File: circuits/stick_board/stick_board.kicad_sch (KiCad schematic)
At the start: 41 parts, among them J1 Conn_01x15_Socket, M2 Motor_DC, Q2 AO3400A, U1 GULI, U2 GULI, U5 DRV5055A1xDBZxQ1, U6 DRV5055A1xDBZxQ1

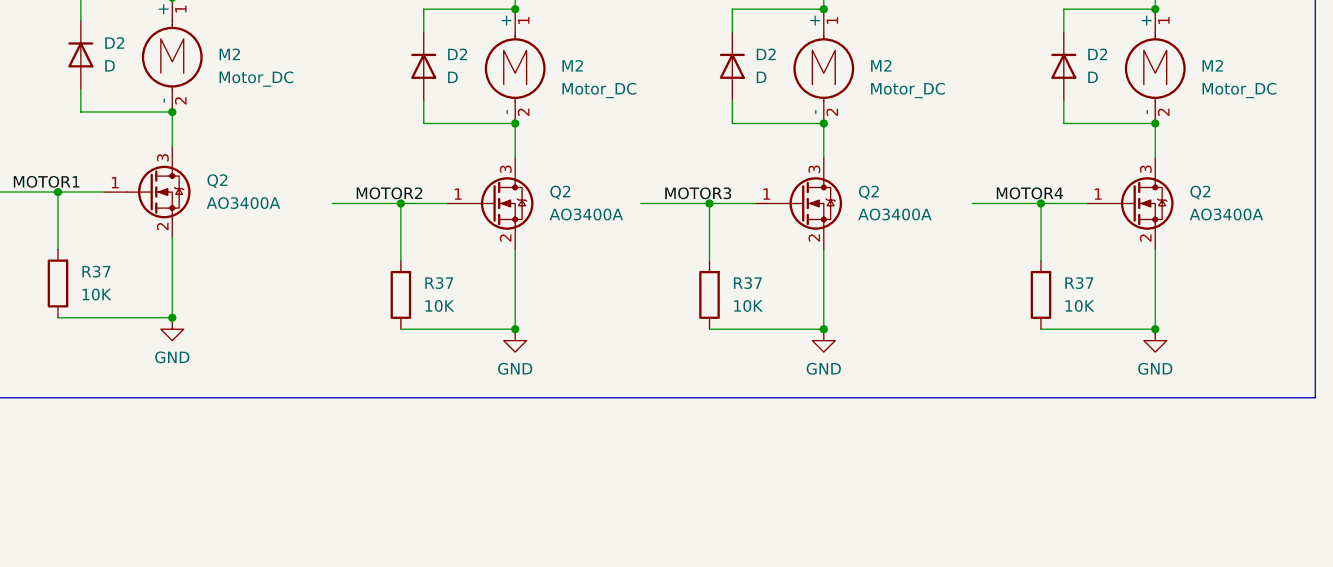
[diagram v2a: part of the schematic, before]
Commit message: 增加马达限流电阻
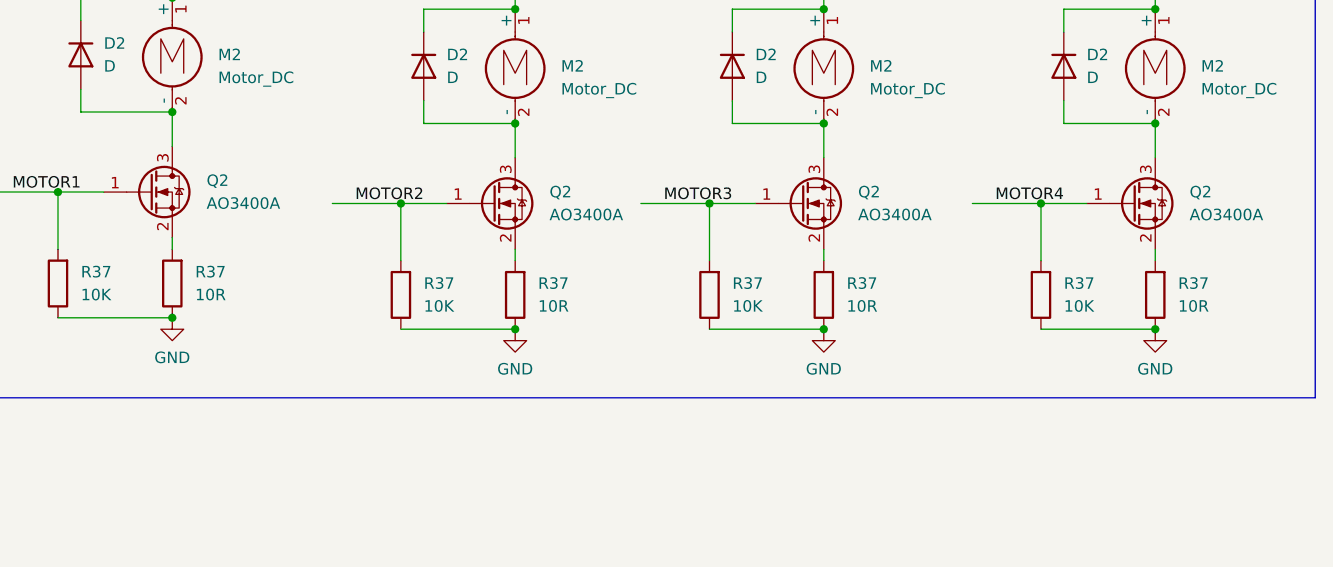
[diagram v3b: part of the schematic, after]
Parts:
- added R37 (x4): 10R, Resistor_SMD:R_0805_2012Metric_Pad1.20x1.40mm_HandSolder, symbol Device:R
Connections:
- net GND: now also R37.1, R37.1, R37.1, R37.1; no longer Q2.2 (S), Q2.2 (S), Q2.2 (S), Q2.2 (S)
- new net: Q2.2 (S), R37.2 (x4)
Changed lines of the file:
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@@
   (junction (at 39.37 187.96) (diameter 0) (color 0 0 0 0)
   )
+  (junction (at 173.99 67.31) (diameter 0) (color 0 0 0 0)
+  )
   (junction (at 245.11 44.45) (diameter 0) (color 0 0 0 0)
   )
   (junction (at 245.11 31.75) (diameter 0) (color 0 0 0 0)
   )
+  (junction (at 135.89 66.04) (diameter 0) (color 0 0 0 0)
+  )
+  (junction (at 38.1 152.4) (diameter 0) (color 0 0 0 0)
+  )
+  (junction (at 20.32 77.47) (diameter 0) (color 0 0 0 0)
+  )
+  (junction (at 173.99 31.75) (diameter 0) (color 0 0 0 0)
+  )
+  (junction (at 161.29 53.34) (diameter 0) (color 0 0 0 0)
+  )
+  (junction (at 135.89 30.48) (diameter 0) (color 0 0 0 0)
+  )
+  (junction (at 135.89 43.18) (diameter 0) (color 0 0 0 0)
+  )
+  (junction (at 208.28 44.45) (diameter 0) (color 0 0 0 0)
+  )
   (junction (at 245.11 67.31) (diameter 0) (color 0 0 0 0)
   )
-  (junction (at 38.1 152.4) (diameter 0) (color 0 0 0 0)
-  )
-  (junction (at 20.32 77.47) (diameter 0) (color 0 0 0 0)
-  )
-  (junction (at 173.99 31.75) (diameter 0) (color 0 0 0 0)
-  )
-  (junction (at 161.29 53.34) (diameter 0) (color 0 0 0 0)
-  )
-  (junction (at 173.99 67.31) (diameter 0) (color 0 0 0 0)
-  )
-  (junction (at 135.89 30.48) (diameter 0) (color 0 0 0 0)
-  )
-  (junction (at 135.89 43.18) (diameter 0) (color 0 0 0 0)
-  )
-  (junction (at 208.28 44.45) (diameter 0) (color 0 0 0 0)
-  )
   (junction (at 20.32 102.87) (diameter 0) (color 0 0 0 0)
   )
+  (junction (at 173.99 44.45) (diameter 0) (color 0 0 0 0)
+  )
+  (junction (at 59.69 102.87) (diameter 0) (color 0 0 0 0)
+  )
+  (junction (at 19.05 48.26) (diameter 0) (color 0 0 0 0)
+  )
+  (junction (at 195.58 53.34) (diameter 0) (color 0 0 0 0)
+  )
+  (junction (at 29.21 21.59) (diameter 0) (color 0 0 0 0)
+  )
   (junction (at 208.28 67.31) (diameter 0) (color 0 0 0 0)
   )
-  (junction (at 135.89 66.04) (diameter 0) (color 0 0 0 0)
-  )
-  (junction (at 173.99 44.45) (diameter 0) (color 0 0 0 0)
-  )
-  (junction (at 59.69 102.87) (diameter 0) (color 0 0 0 0)
-  )
-  (junction (at 19.05 48.26) (diameter 0) (color 0 0 0 0)
-  )
-  (junction (at 195.58 53.34) (diameter 0) (color 0 0 0 0)
-  )
-  (junction (at 29.21 21.59) (diameter 0) (color 0 0 0 0)
-  )
   (junction (at 17.78 21.59) (diameter 0) (color 0 0 0 0)
   )
@@
     (stroke (width 0) (type default))
   )
+  (wire (pts (xy 173.99 58.42) (xy 173.99 59.69))
+    (stroke (width 0) (type default))
+  )
   (wire (pts (xy 30.48 157.48) (xy 34.29 157.48))
     (stroke (width 0) (type default))
@@
     (stroke (width 0) (type default))
   )
-  (wire (pts (xy 135.89 57.15) (xy 135.89 66.04))
-    (stroke (width 0) (type default))
-  )
   (wire (pts (xy 33.02 16.51) (xy 29.21 16.51))
     (stroke (width 0) (type default))
@@
     (stroke (width 0) (type default))
   )
-  (wire (pts (xy 245.11 58.42) (xy 245.11 67.31))
-    (stroke (width 0) (type default))
-  )
   (wire (pts (xy 29.21 21.59) (xy 29.21 16.51))
     (stroke (width 0) (type default))
@@
     (stroke (width 0) (type default))
   )
-  (wire (pts (xy 208.28 58.42) (xy 208.28 67.31))
-    (stroke (width 0) (type default))
-  )
   (wire (pts (xy 161.29 53.34) (xy 166.37 53.34))
     (stroke (width 0) (type default))
   )
+  (wire (pts (xy 135.89 57.15) (xy 135.89 58.42))
+    (stroke (width 0) (type default))
+  )
   (wire (pts (xy 59.69 99.06) (xy 59.69 102.87))
     (stroke (width 0) (type default))
   )
-  (wire (pts (xy 173.99 58.42) (xy 173.99 67.31))
-    (stroke (width 0) (type default))
-  )
   (wire (pts (xy 173.99 27.94) (xy 173.99 31.75))
     (stroke (width 0) (type default))
@@
   )
   (wire (pts (xy 33.02 41.91) (xy 29.21 41.91))
+    (stroke (width 0) (type default))
+  )
+  (wire (pts (xy 245.11 58.42) (xy 245.11 59.69))
+    (stroke (width 0) (type default))
+  )
+  (wire (pts (xy 208.28 58.42) (xy 208.28 59.69))
     (stroke (width 0) (type default))
   )
@@
   (label "MOTOR2" (at 156.21 53.34 0) (fields_autoplaced)
     (effects (font (size 1.27 1.27)) (justify left bottom))
+  )
+  (symbol (lib_id "Device:R") (at 245.11 63.5 180) (unit 1)
+    (in_bom yes) (on_board yes) (dnp no) (fields_autoplaced)
+    (property "Reference" "R37" (at 247.65 62.23 0)
+      (effects (font (size 1.27 1.27)) (justify right))
+    )
+    (property "Value" "10R" (at 247.65 64.77 0)
+      (effects (font (size 1.27 1.27)) (justify right))
+    )
+    (property "Footprint" "Resistor_SMD:R_0805_2012Metric_Pad1.20x1.40mm_HandSolder" (at 246.888 63.5 90)
+      (effects (font (size 1.27 1.27)) hide)
+    )
+    (property "Datasheet" "~" (at 245.11 63.5 0)
+      (effects (font (size 1.27 1.27)) hide)
+    )
+    (pin "1")
+    (pin "2")
+    (instances
+      (project "testpad"
+        (path "/2275f0ad-bf55-4256-a734-efa72019bc53"
+          (reference "R37") (unit 1)
+        )
+      )
+      (project "stick_board"
+        (path "/ee025c96-6b34-4741-98da-90887f64560f"
+          (reference "R23") (unit 1)
+        )
+      )
+    )
   )
   (symbol (lib_id "stick:GULI") (at 38.1 52.07 0) (unit 1)
@@
     )
   )
+  (symbol (lib_id "Device:R") (at 208.28 63.5 180) (unit 1)
+    (in_bom yes) (on_board yes) (dnp no) (fields_autoplaced)
+    (property "Reference" "R37" (at 210.82 62.23 0)
+      (effects (font (size 1.27 1.27)) (justify right))
+    )
+    (property "Value" "10R" (at 210.82 64.77 0)
+      (effects (font (size 1.27 1.27)) (justify right))
+    )
+    (property "Footprint" "Resistor_SMD:R_0805_2012Metric_Pad1.20x1.40mm_HandSolder" (at 210.058 63.5 90)
+      (effects (font (size 1.27 1.27)) hide)
+    )
+    (property "Datasheet" "~" (at 208.28 63.5 0)
+      (effects (font (size 1.27 1.27)) hide)
+    )
+    (pin "1")
+    (pin "2")
+    (instances
+      (project "testpad"
+        (path "/2275f0ad-bf55-4256-a734-efa72019bc53"
+          (reference "R37") (unit 1)
+        )
+      )
+      (project "stick_board"
+        (path "/ee025c96-6b34-4741-98da-90887f64560f"
+          (reference "R22") (unit 1)
+        )
+      )
+    )
+  )
   (symbol (lib_id "Sensor_Magnetic:DRV5055A1xDBZxQ1") (at 30.48 87.63 0) (unit 1)
     (in_bom yes) (on_board yes) (dnp no)
@@
         (path "/ee025c96-6b34-4741-98da-90887f64560f"
           (reference "#PWR013") (unit 1)
+        )
+      )
+    )
+  )
+  (symbol (lib_id "Device:R") (at 135.89 62.23 180) (unit 1)
+    (in_bom yes) (on_board yes) (dnp no) (fields_autoplaced)
+    (property "Reference" "R37" (at 138.43 60.96 0)
+      (effects (font (size 1.27 1.27)) (justify right))
+    )
+    (property "Value" "10R" (at 138.43 63.5 0)
+      (effects (font (size 1.27 1.27)) (justify right))
+    )
+    (property "Footprint" "Resistor_SMD:R_0805_2012Metric_Pad1.20x1.40mm_HandSolder" (at 137.668 62.23 90)
+      (effects (font (size 1.27 1.27)) hide)
+    )
+    (property "Datasheet" "~" (at 135.89 62.23 0)
+      (effects (font (size 1.27 1.27)) hide)
+    )
+    (pin "1")
+    (pin "2")
+    (instances
+      (project "testpad"
+        (path "/2275f0ad-bf55-4256-a734-efa72019bc53"
+          (reference "R37") (unit 1)
+        )
+      )
+      (project "stick_board"
+        (path "/ee025c96-6b34-4741-98da-90887f64560f"
+          (reference "R20") (unit 1)
         )
       )
@@
         )
       )
+    )
+  )
+  (symbol (lib_id "Device:R") (at 173.99 63.5 180) (unit 1)
+    (in_bom yes) (on_board yes) (dnp no) (fields_autoplaced)
+    (property "Reference" "R37" (at 176.53 62.23 0)
+      (effects (font (size 1.27 1.27)) (justify right))
+    )
+    (property "Value" "10R" (at 176.53 64.77 0)
+      (effects (font (size 1.27 1.27)) (justify right))
+    )
+    (property "Footprint" "Resistor_SMD:R_0805_2012Metric_Pad1.20x1.40mm_HandSolder" (at 175.768 63.5 90)
+      (effects (font (size 1.27 1.27)) hide)
+    )
+    (property "Datasheet" "~" (at 173.99 63.5 0)
+      (effects (font (size 1.27 1.27)) hide)
+    )
+    (pin "1")
+    (pin "2")
+    (instances
+      (project "testpad"
+        (path "/2275f0ad-bf55-4256-a734-efa72019bc53"
+          (reference "R37") (unit 1)
+        )
+      )
+      (project "stick_board"
+        (path "/ee025c96-6b34-4741-98da-90887f64560f"
+          (reference "R21") (unit 1)
+        )
+      )

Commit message: layout 摇杆板布局ok
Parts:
- removed D2 (x2): D, Diode_SMD:D_0805_2012Metric_Pad1.15x1.40mm_HandSolder, symbol Device:D
- removed J1: Conn_01x15_Socket, symbol Connector:Conn_01x15_Socket
- removed M2 (x2): Motor_DC, Resistor_SMD:R_1210_3225Metric_Pad1.30x2.65mm_HandSolder, symbol Motor:Motor_DC
- removed Q2 (x2): AO3400A, Package_TO_SOT_SMD:SOT-23-3, symbol Transistor_FET:AO3400A
- removed R10, R11, R12, R17, R18, R19, R3, R4, R5, R6, R7, R8, R9: 22R, symbol Device:R
- removed R37 (x2): 10R, Resistor_SMD:R_0805_2012Metric_Pad1.20x1.40mm_HandSolder, symbol Device:R
- removed R37 (x2): 10K, Resistor_SMD:R_0805_2012Metric_Pad1.20x1.40mm_HandSolder, symbol Device:R
- added J1: Conn_01x13_Pin, Connector_FFC-FPC:Molex_200528-0130_1x13-1MP_P1.00mm_Horizontal, symbol Connector:Conn_01x13_Pin
- R1, R2: footprint (none) -> Resistor_SMD:R_0805_2012Metric_Pad1.20x1.40mm_HandSolder
- R37: footprint Resistor_SMD:R_0805_2012Metric_Pad1.20x1.40mm_HandSolder -> Resistor_SMD:R_1206_3216Metric_Pad1.30x1.75mm_HandSolder
- SW_Push1: value SW_RST -> SW_PUSH; footprint Button_Switch_THT:SW_PUSH_6mm_H4.3mm -> stick:touch
- U1, U2: footprint (none) -> stick:GULI
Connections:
- net +3V3: now also J1.13 (Pin_13)
- net BTN_B: now also J1.3 (Pin_3)
- net GND: now also J1.1 (Pin_1)
- net LEFT_BTN: now also J1.9 (Pin_9)
- net LEFT_HALL: now also J1.10 (Pin_10)
- net LEFT_X: now also J1.12 (Pin_12)
- net LEFT_Y: now also J1.11 (Pin_11)
- net MOTOR1: now also J1.8 (Pin_8)
- net MOTOR2: now also J1.2 (Pin_2)
- net RIGHT_BTN: now also J1.4 (Pin_4)
- net RIGHT_HALL: now also J1.5 (Pin_5)
- net RIGHT_X: now also J1.7 (Pin_7)
- net RIGHT_Y: now also J1.6 (Pin_6)

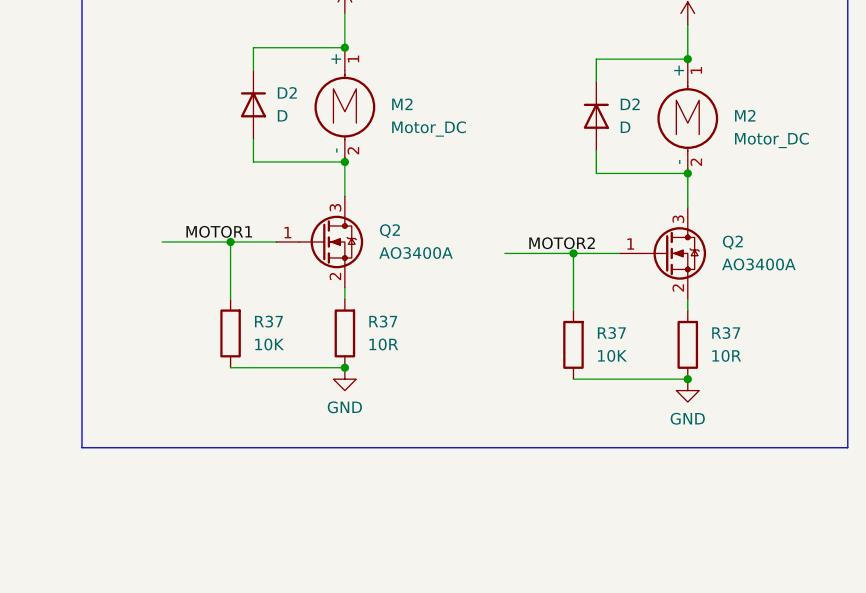
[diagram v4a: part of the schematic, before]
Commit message: layout  摇杆板优化马达驱动,增加覆铜过孔         MCU板改动
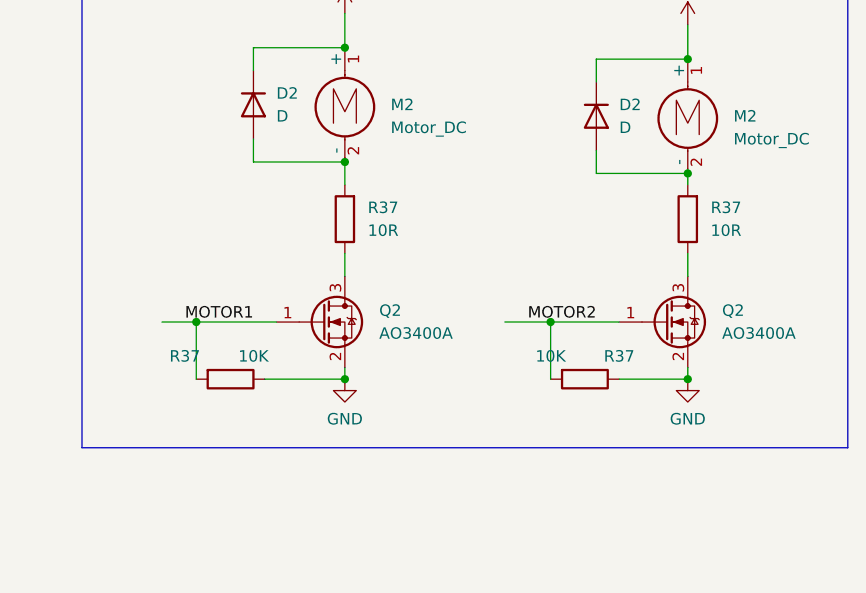
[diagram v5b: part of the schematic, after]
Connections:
- net GND: now also Q2.2 (S), Q2.2 (S); no longer R37.1, R37.1
- net at D2.2 (A), M2.2 (-): now also R37.2; no longer Q2.3 (D) (x2)
- new net: Q2.3 (D), R37.1 (x2)
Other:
- moved on the sheet: Q2, R37
